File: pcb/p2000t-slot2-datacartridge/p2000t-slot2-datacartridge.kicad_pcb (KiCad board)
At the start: 4 copper layers, 80 x 100 mm, 27 parts, among them J1 P2000T Port 2, U1 74HC04, U11 CY62256-70PC, U13 74HC173, U14 ZIF, U15 74HC02, U3 74HC138, U4 74HC21, U5 SST39SF040, U6 74HC02, U8 74HC273, U9 74HC273

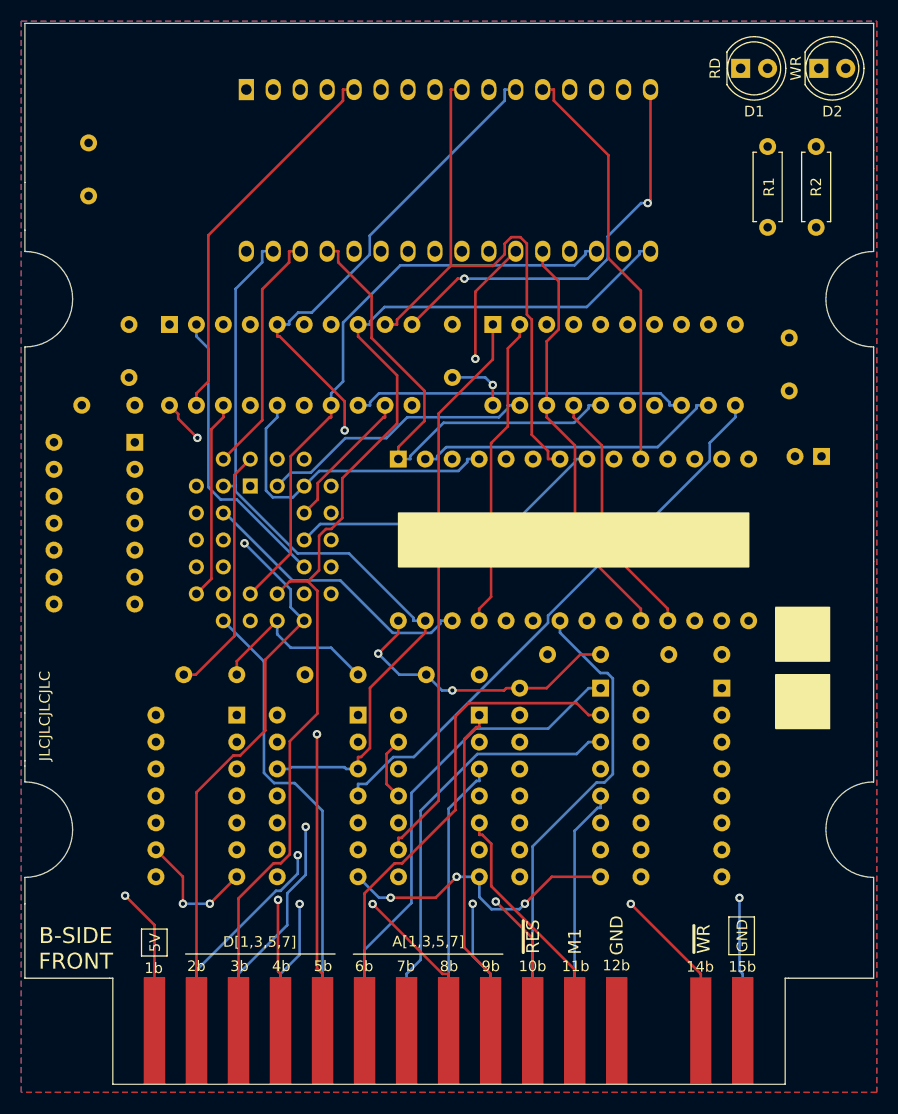
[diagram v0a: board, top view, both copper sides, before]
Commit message: Patch 0.3.0 (#9)
* Improving lay-out board

* Fixing incorrect layer in gerber files

* Initial commit rev2 and implementing LEDs in firmware flasher

* Fixing bug that triggered undefined behavior when writing to FAT chip

* Fixing incorrect RES line

* Building rev2 of the data cartridge

* Refactoring serial interface

* Adding leds to launcher

* Adding new emulator

* Expanding README

* Adding .dll files

* Adding missing files

* Adding LEDs to launcher

* Fixing bugs, adding icons, adding explainers
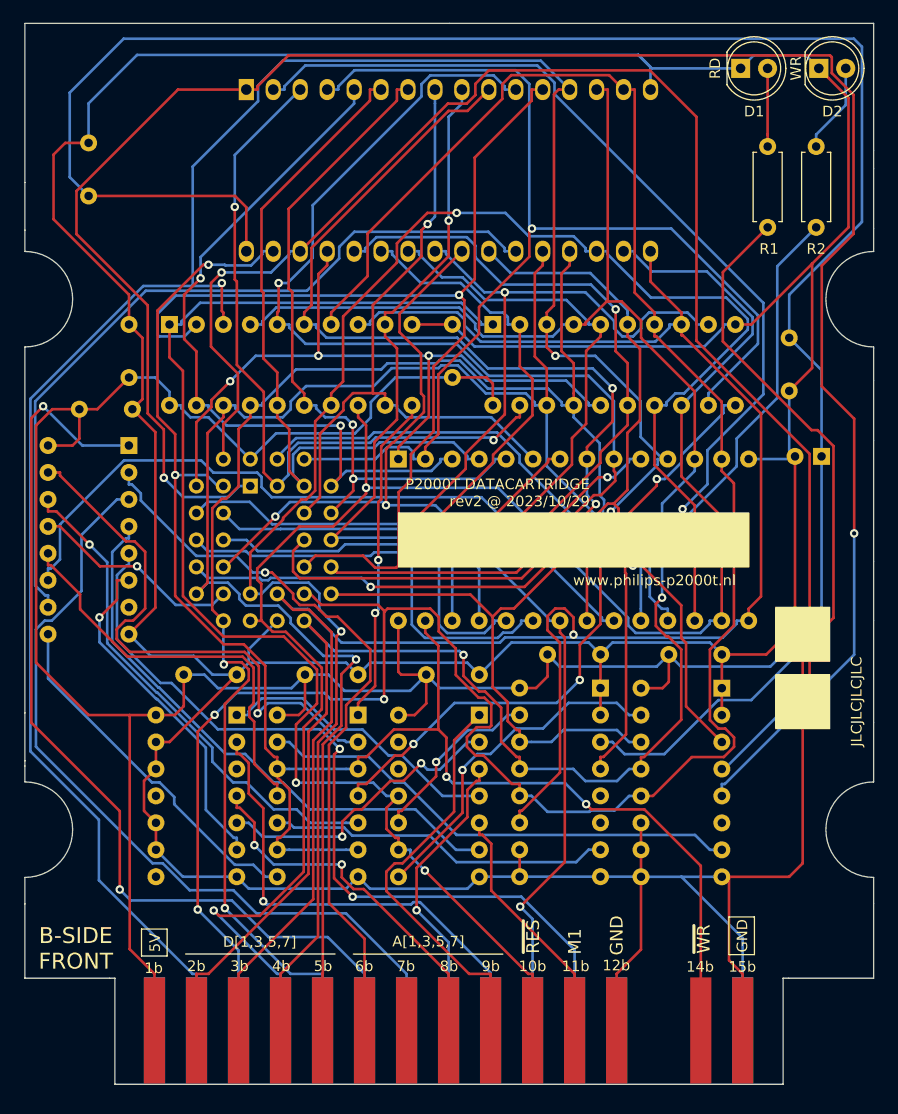
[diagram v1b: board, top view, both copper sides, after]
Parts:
- removed U15: 74HC02, Package_DIP:DIP-14_W7.62mm_Socket
- added U9: 74HC173, Package_DIP:DIP-16_W7.62mm_Socket, B.Cu at (97.8, 115.6)
- moved U3 50.0 mm to (53.3, 92.7)
- moved C6 5.24 mm to (48.7, 89.3), turned to 0 degrees
- moved C10 5.00 mm to (92.8, 112.4), turned to 0 degrees
- renumbered U6 to U1, U14 to U10, U1 to U2, U8 to U5, U9 to U6, U13 to U7, U5 to U8
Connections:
- U1 pad 10: unconnected-(U6-Pad10) -> Net-(U1-Pad10)
- U1 pad 8: VCC -> SO6
- U1 pad 9: VCC -> ~{WR}
- U2 pad 10: unconnected-(U1-Pad10) -> Net-(U2-Pad10)
- U2 pad 11: VCC -> ~{RES}
- U2 pad 12: unconnected-(U1-Pad12) -> (no net)
- U2 pad 13: VCC -> (no net)
- U3 pad 9: unconnected-(U3-Pad9) -> SO6
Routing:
- net GND: track 109.2 -> 487.1 mm, vias 8 -> 0
- net VCC: track 87.1 -> 392.2 mm, vias 5 -> 0
- net D0: track 184.2 -> 253.2 mm, vias 1 -> 3
- net CA17: track 84.6 -> 144.4 mm, vias 0 -> 2
- net SO5: track 132.2 -> 73.6 mm, vias 1 -> 0
- net ~{IORQ}: track 23.3 -> 79.4 mm, vias 0 -> 2
- net CA16: track 91.5 -> 147.6 mm, vias 0 -> 2
- net CA18: track 147.4 -> 194.8 mm, vias 0 -> 2
- net D3: track 148.5 -> 194.9 mm, vias 0 -> 1
- net A0: track 46.1 -> 90.8 mm, vias 0 -> 2
- net SO4: track 23.4 -> 67.6 mm
- net Net-(U2-Pad6): track 14.8 -> 54.4 mm
- net Net-(R2-Pad1): track 97.5 -> 60.6 mm, vias 0 -> 1
- net Net-(U1-Pad2): track 16.3 -> 52.5 mm, vias 0 -> 1
- net A2: track 40.9 -> 77.1 mm
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- removed copper zone on F.Cu, net GND
- removed copper zone on B.Cu, net VCC
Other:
- outline, holes or cut-outs redrawn
- copper layers 4 -> 2
- board text added: "P2000T DATACARTRIDGE rev2 @ 2023/10/29"
- board text added: "www.philips-p2000t.nl"

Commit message: Revision 3 and 4 of the PCB (#12)
* Initial commit revision

* Interim commit

* Rerouting

* Fixing bug in PCB
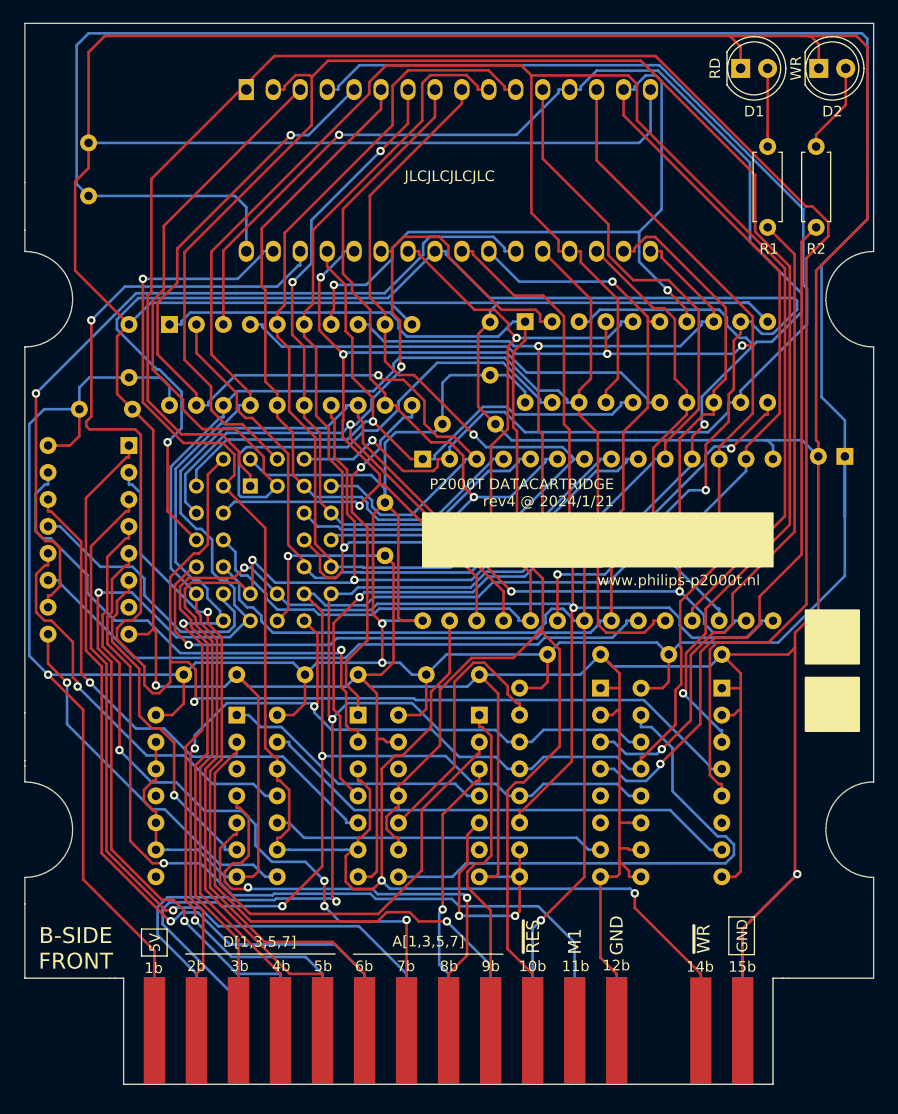
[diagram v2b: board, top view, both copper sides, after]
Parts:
- added C12: 0.1uF, Capacitor_THT:C_Disc_D5.0mm_W2.5mm_P5.00mm, B.Cu at (77.5, 98.1)
- moved C8 33.7 mm to (82.9, 90.7), turned to 0 degrees
- moved C7 3.56 mm to (87.4, 86.1)
- moved U5 3.05 mm to (90.7, 81.0)
- moved U11 2.30 mm to (81.0, 94.0)
- moved C11 2.20 mm to (120.8, 93.7)
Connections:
- J1 pad 11b: M1 -> unconnected-(J1-Pin_11b-Pad11b)
- J1 pad 7b: unconnected-(J1-Pad7b) -> A3
- U2 pad 12: (no net) -> unconnected-(U2-Pad12)
- U2 pad 13: (no net) -> GND
- U2 pad 5: M1 -> GND
- U2 pad 6: Net-(U2-Pad6) -> unconnected-(U2-Pad6)
- U3 pad 4: Net-(U2-Pad6) -> A3
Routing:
- net GND: track 487.1 -> 714.8 mm, vias 0 -> 5
- net D6: track 143.8 -> 239.8 mm
- net A3: track 0.00 -> 69.7 mm, vias 0 -> 4
- net Net-(U2-Pad6): track 54.4 -> 0.00 mm
- net VCC: track 392.2 -> 439.1 mm, vias 0 -> 3
- net CA11: track 100.4 -> 141.9 mm, vias 2 -> 3
- net D4: track 168.0 -> 195.4 mm, vias 2 -> 4
- net M1: track 23.4 -> 0.00 mm
- net CA15: track 69.7 -> 93.0 mm, vias 2 -> 0
- net CA18: track 194.8 -> 173.1 mm, vias 2 -> 0
- net CA7: track 70.1 -> 89.8 mm
- net Net-(U7-Mr): track 32.6 -> 50.3 mm, vias 1 -> 0
- net D2: track 229.3 -> 246.2 mm, vias 3 -> 4
- net CA2: track 109.5 -> 94.5 mm, vias 2 -> 1
- net Net-(U2-Pad2): track 28.4 -> 42.9 mm, vias 2 -> 0
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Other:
- outline, holes or cut-outs redrawn
- board text added: "P2000T DATACARTRIDGE rev4 @ 2024/1/21"
- board text removed: "P2000T DATACARTRIDGE rev2 @ 2023/10/29"
